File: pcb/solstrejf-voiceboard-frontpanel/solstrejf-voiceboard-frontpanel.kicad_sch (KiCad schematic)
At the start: 13 parts, among them J1 Conn_02x08_Odd_Even, SW1 TRIG

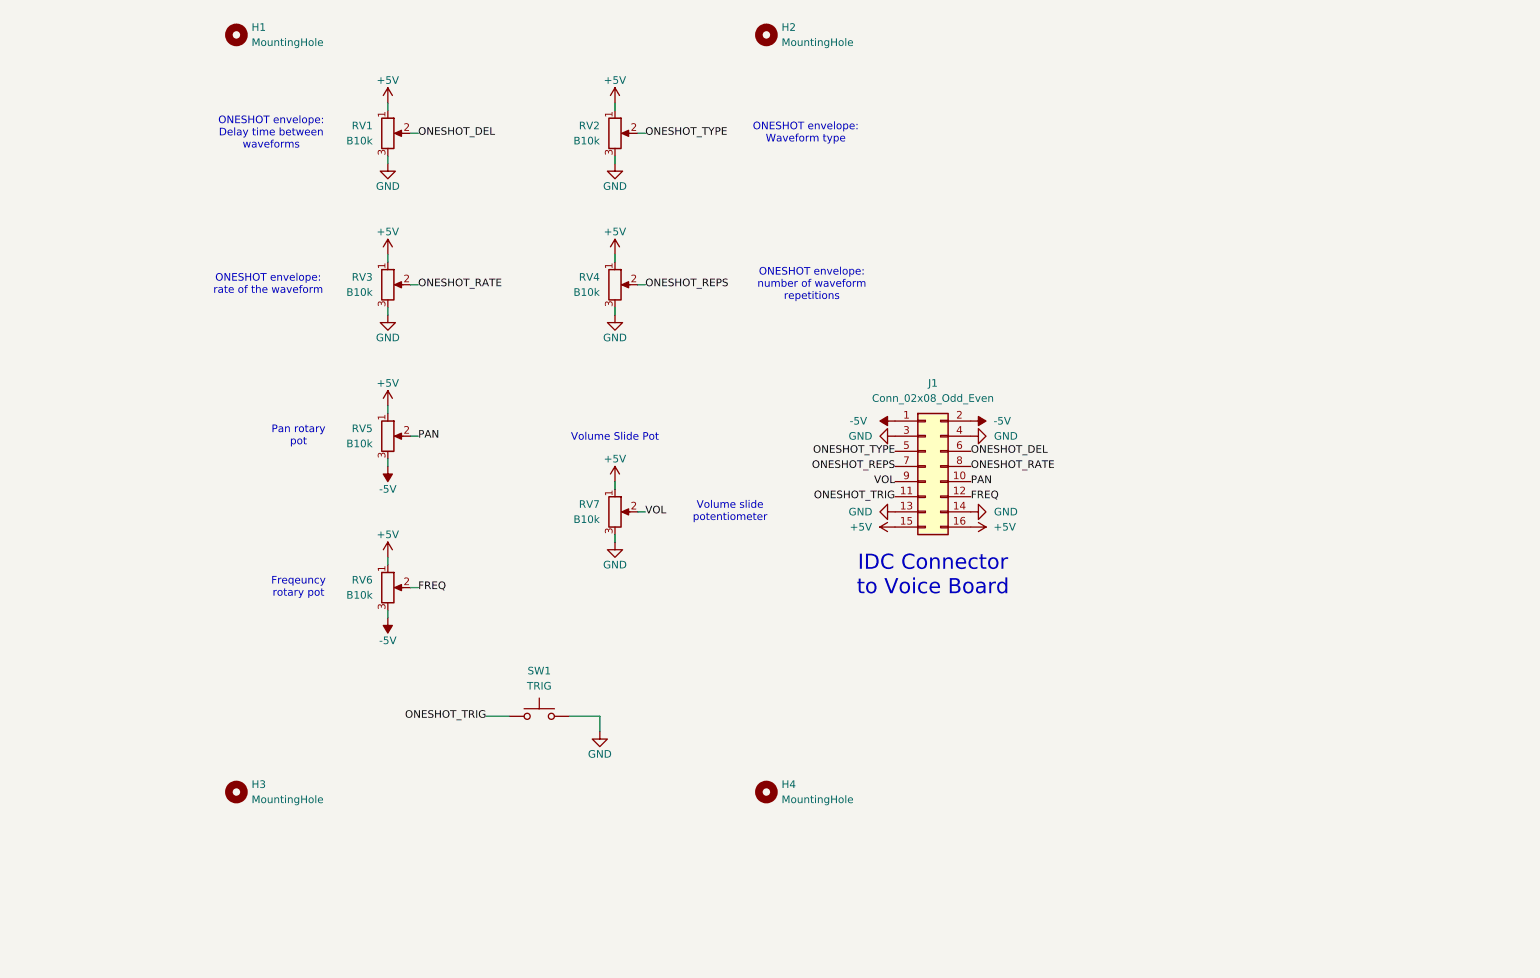
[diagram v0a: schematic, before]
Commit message: updated Kromftronics submodule name and edited path in all PCB projects. Added work-in-progress for the front-panel PCB and the small updates in the voice-board schematic
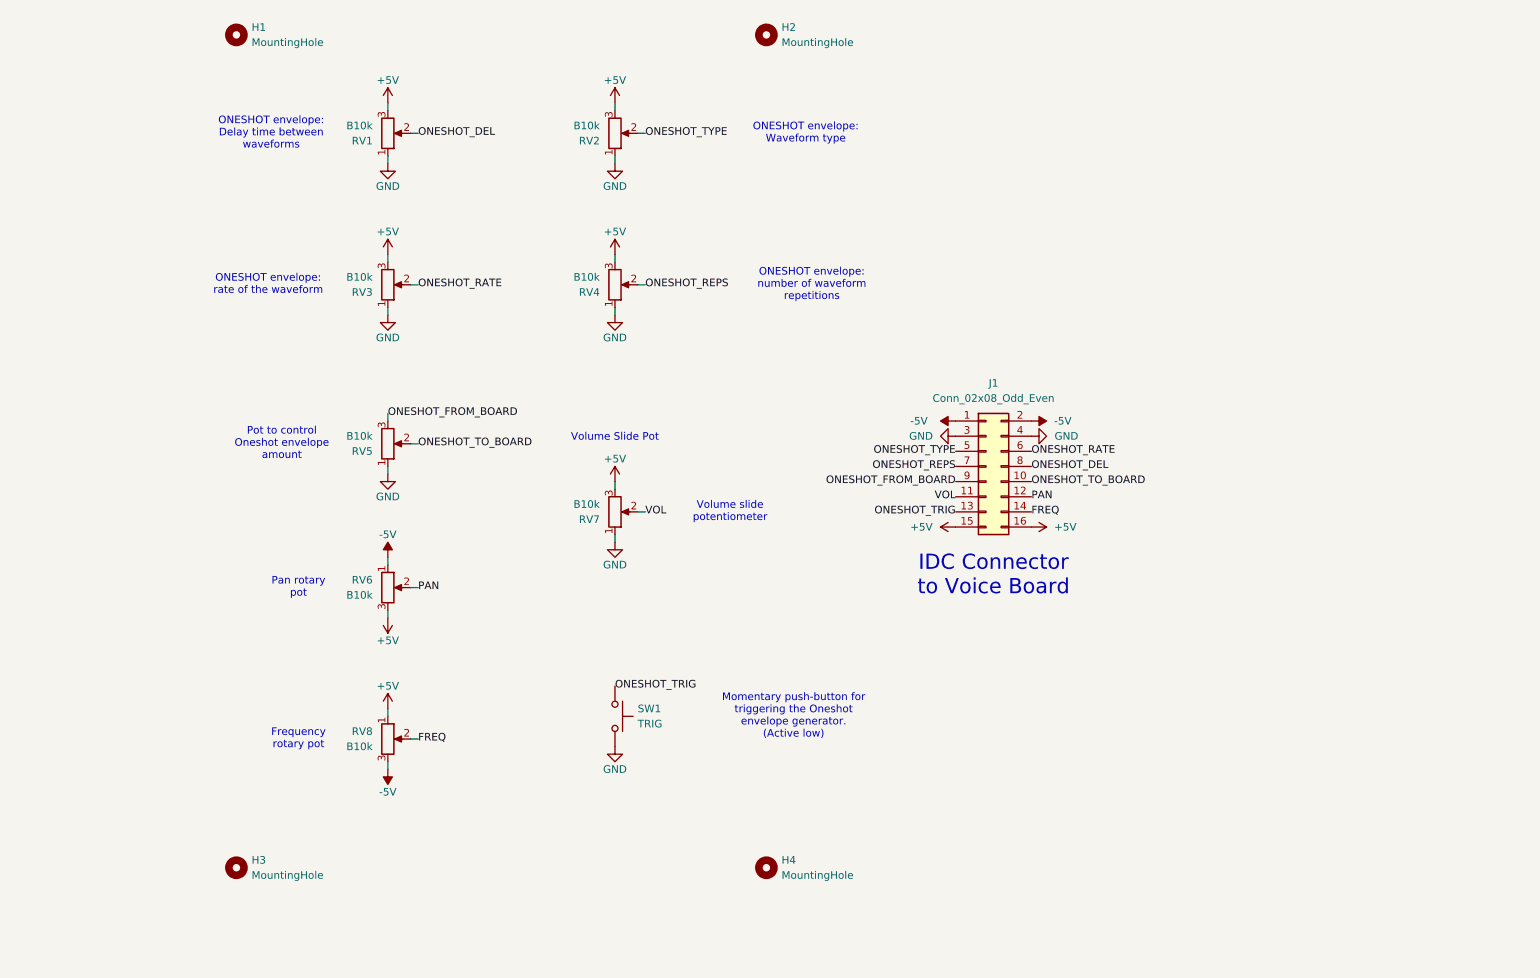
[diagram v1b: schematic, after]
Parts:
- added RV5: B10k, Potentiometer_THT:Potentiometer_Alpha_RD901F-40-00D_Single_Vertical, symbol Device:R_Potentiometer
- renumbered RV5 to RV6, RV6 to RV8
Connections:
- net +5V: now also RV1.3, RV2.3, RV3.3, RV4.3, RV6.3, RV7.3; no longer RV1.1, RV2.1, RV3.1, RV4.1, RV6.1, RV7.1
- net -5V: now also RV6.1; no longer RV6.3
- net FREQ: now also J1.14 (Pin_14); no longer J1.12 (Pin_12)
- net GND: now also RV1.1, RV2.1, RV3.1, RV4.1, RV7.1, RV5.1; no longer J1.13 (Pin_13), J1.14 (Pin_14), RV1.3, RV2.3, RV3.3, RV4.3, RV7.3
- net ONESHOT_DEL: now also J1.8 (Pin_8); no longer J1.6 (Pin_6)
- net ONESHOT_RATE: now also J1.6 (Pin_6); no longer J1.8 (Pin_8)
- net ONESHOT_TRIG: now also J1.13 (Pin_13); no longer J1.11 (Pin_11)
- net PAN: now also J1.12 (Pin_12); no longer J1.10 (Pin_10)
- net VOL: now also J1.11 (Pin_11); no longer J1.9 (Pin_9)
- new net ONESHOT_FROM_BOARD: J1.9 (Pin_9), RV5.3
- new net ONESHOT_TO_BOARD: J1.10 (Pin_10), RV5.2
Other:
- note added: "Frequency rotary pot"
- note added: "Momentary push-button for triggering the Oneshot envelope generator. (Active low)"
- note added: "Pot to control Oneshot envelope amount"
- note removed: "Freqeuncy rotary pot"
- moved on the sheet: H3, H4, J1, RV6, RV8, SW1

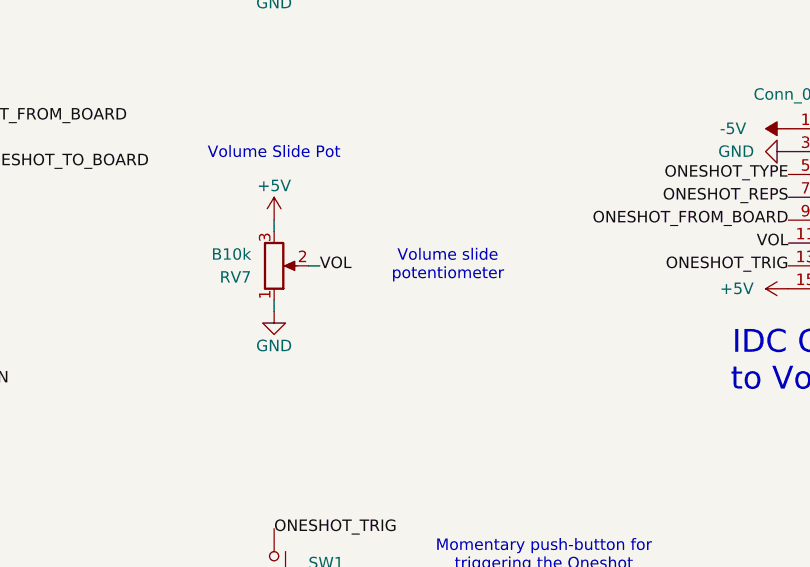
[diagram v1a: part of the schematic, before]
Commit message: Found an error in the front panel where the volume pot was inverted. Updated the schematics of the voice board core and front panel.
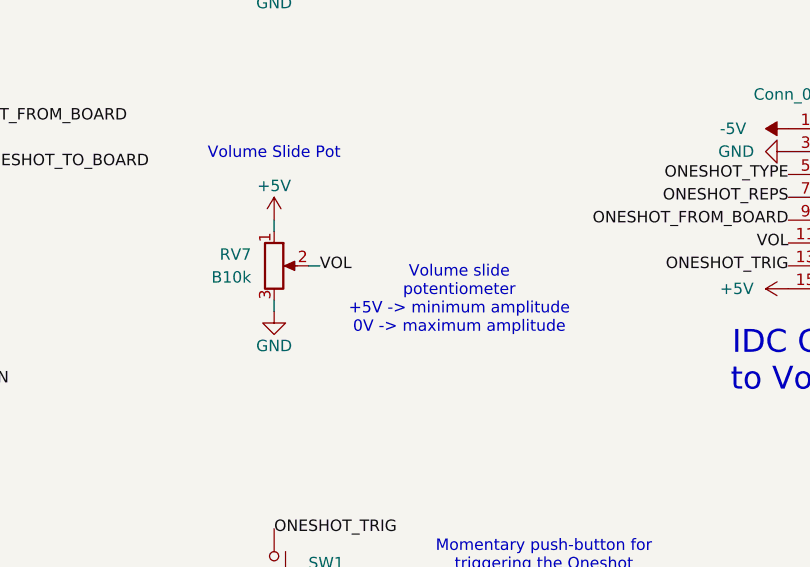
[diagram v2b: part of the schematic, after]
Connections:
- net +5V: now also RV7.1; no longer RV7.3
- net GND: now also RV7.3; no longer RV7.1
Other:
- note added: "Volume slide potentiometer +5V -> minimum amplitude 0V -> maximum amplitude"
- note removed: "Volume slide potentiometer"
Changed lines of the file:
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@@
 	(title_block
 		(title "Solstrejf Voice Board Front Panel")
-		(date "2024-08-31")
+		(date "2024-10-28")
 		(rev "REV 1.0")
 	)
@@
 		)
 	)
-	(text "Volume slide\npotentiometer"
-		(exclude_from_sim no)
-		(at 146.304 118.11 0)
+	(text "Volume slide\npotentiometer\n+5V -> minimum amplitude\n0V -> maximum amplitude"
+		(exclude_from_sim no)
+		(at 147.574 121.92 0)
 		(effects
 			(font
@@
 		(lib_id "Device:R_Potentiometer")
 		(at 127 118.11 0)
-		(mirror x)
-		(unit 1)
-		(exclude_from_sim no)
-		(in_bom yes)
-		(on_board yes)
-		(dnp no)
-		(fields_autoplaced yes)
+		(unit 1)
+		(exclude_from_sim no)
+		(in_bom yes)
+		(on_board yes)
+		(dnp no)
 		(property "Reference" "RV7"
-			(at 124.46 119.3801 0)
+			(at 124.46 116.8399 0)
 			(effects
 				(font
@@
 		)
 		(property "Value" "B10k"
-			(at 124.46 116.8401 0)
-			(effects
-				(font
+			(at 124.46 119.3799 0)
+			(effects
+				(font

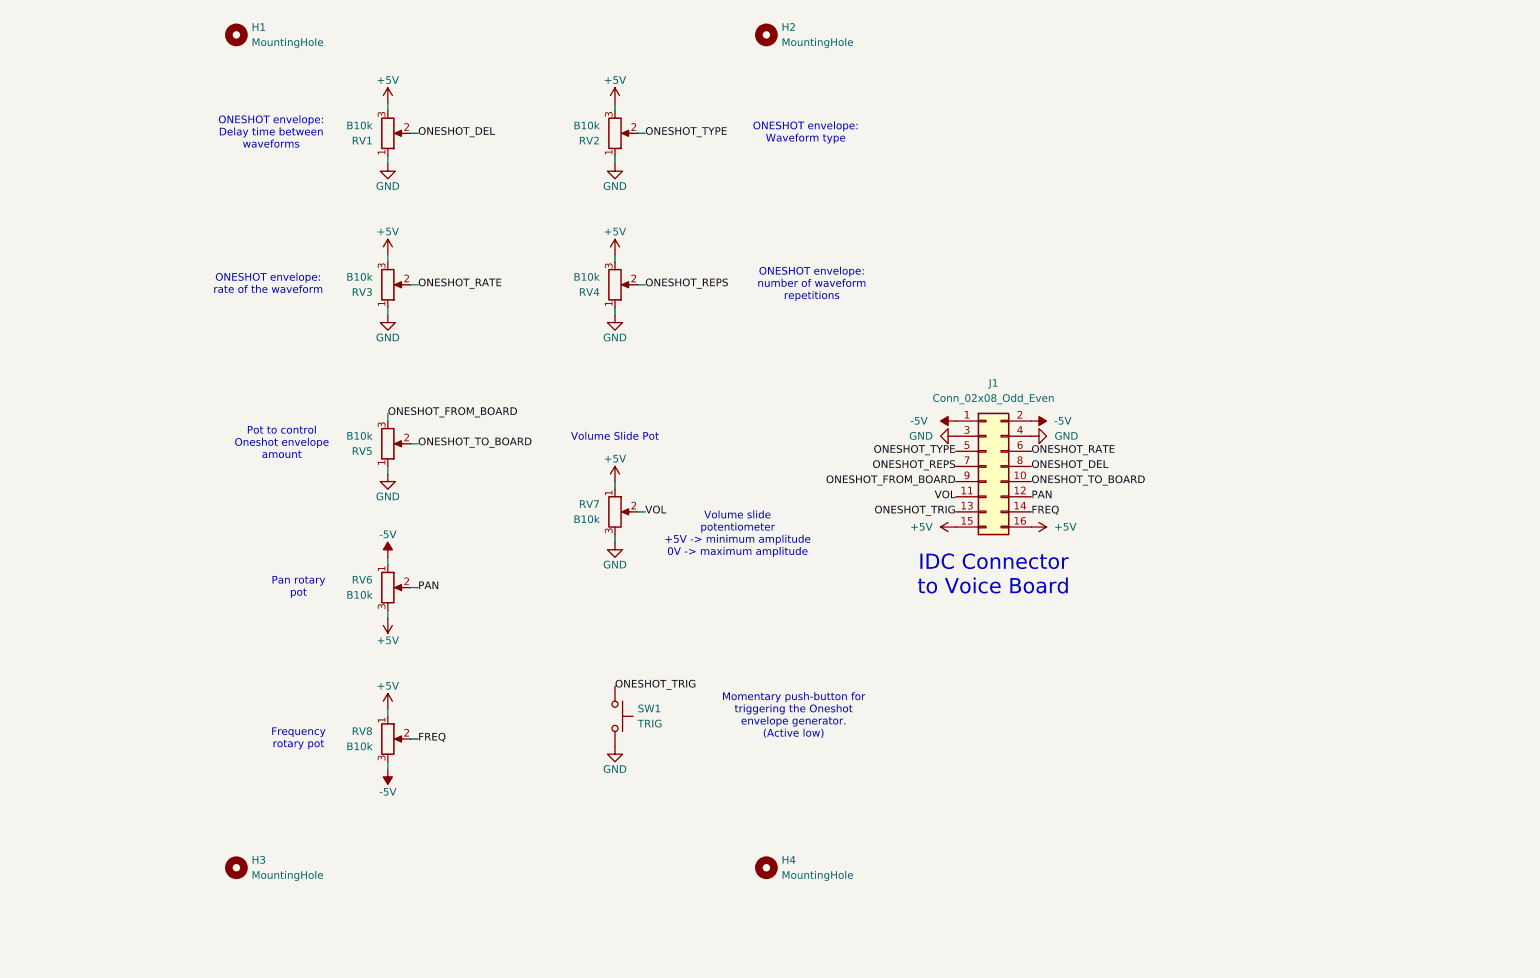
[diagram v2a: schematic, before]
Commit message: updated frontpanel to rev2
- added a external trigger input for PIR motion sensor
- added a 0-5V 1V/oct cv input to the frequency cv
- PCB DRC clean
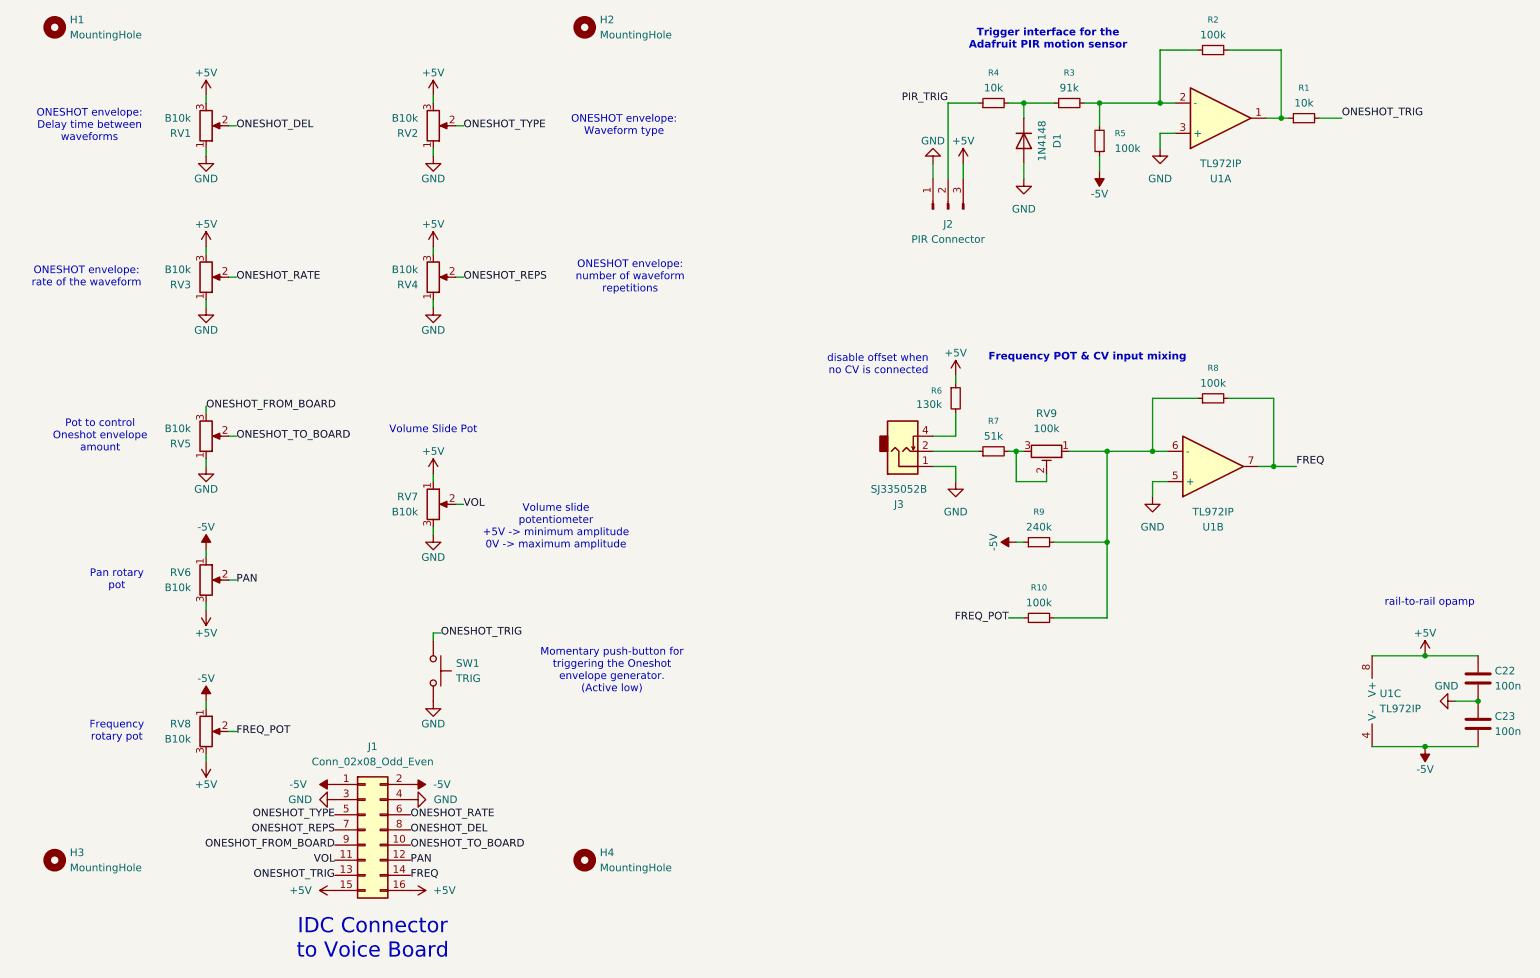
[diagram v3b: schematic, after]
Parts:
- added C22, C23: 100n, Capacitor_THT:C_Disc_D5.0mm_W2.5mm_P5.00mm, symbol Device:C
- added D1: 1N4148, Diode_THT:D_DO-35_SOD27_P7.62mm_Horizontal, symbol Diode:1N4148
- added J2: PIR Connector, Connector_PinHeader_2.54mm:PinHeader_1x03_P2.54mm_Vertical, symbol Connector:Conn_01x03_Pin
- added J3: SJ335052B, Kromftronics_Custom:SJ335052B, symbol Connector_Audio:AudioJack2_SwitchT
- added R1, R4: 10k, Resistor_THT:R_Axial_DIN0207_L6.3mm_D2.5mm_P10.16mm_Horizontal, symbol Device:R_Small
- added R10, R2, R5, R8: 100k, Resistor_THT:R_Axial_DIN0207_L6.3mm_D2.5mm_P10.16mm_Horizontal, symbol Device:R_Small
- added R3: 91k, Resistor_THT:R_Axial_DIN0207_L6.3mm_D2.5mm_P10.16mm_Horizontal, symbol Device:R_Small
- added R6: 130k, Resistor_THT:R_Axial_DIN0207_L6.3mm_D2.5mm_P10.16mm_Horizontal, symbol Device:R_Small
- added R7: 51k, Resistor_THT:R_Axial_DIN0207_L6.3mm_D2.5mm_P10.16mm_Horizontal, symbol Device:R_Small
- added R9: 240k, Resistor_THT:R_Axial_DIN0207_L6.3mm_D2.5mm_P10.16mm_Horizontal, symbol Device:R_Small
- added RV9: 100k, Potentiometer_THT:Potentiometer_Bourns_3296Y_Vertical, symbol Device:R_Potentiometer_Trim
- added U1: TL972IP, Package_DIP:DIP-8_W7.62mm_Socket, symbol Device:Opamp_Dual
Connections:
- net +5V: now also RV8.3, C22.1, J2.3 (Pin_3), R6.1, U1.8 (V+); no longer RV8.1
- net -5V: now also RV8.1, C23.2, R5.1, R9.1, U1.4 (V-); no longer RV8.3
- net FREQ: now also R8.2, U1.7; no longer RV8.2
- net GND: now also C22.2, C23.1, D1.2 (A), J2.1 (Pin_1), J3.1, U1.3 (+), U1.5 (+)
- net ONESHOT_TRIG: now also R1.2
- new net: R10.2, R8.1, R9.2, RV9.1, U1.6 (-)
- new net: D1.1 (K), R3.1, R4.2
- new net: R2.1, R3.2, R5.2, U1.2 (-)
- new net: J3.4, R6.2
- new net: J3.2, R7.1
- new net: R7.2, RV9.2, RV9.3
- new net: R1.1, R2.2, U1.1
- new net FREQ_POT: R10.1, RV8.2
- new net PIR_TRIG: J2.2 (Pin_2), R4.1
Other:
- note added: "Frequency POT & CV input mixing"
- note added: "Trigger interface for the Adafruit PIR motion sensor"
- note added: "disable offset when no CV is connected"
- note added: "rail-to-rail opamp"
- moved on the sheet: H1, H2, H3, H4, J1, RV1, RV2, RV3, RV4, RV5, RV6, RV7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

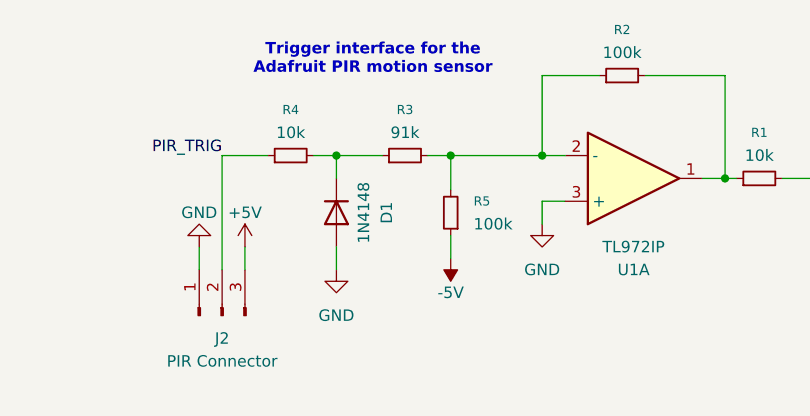
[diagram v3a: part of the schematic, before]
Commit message: updated frontpanel resistor value and added 3D renders
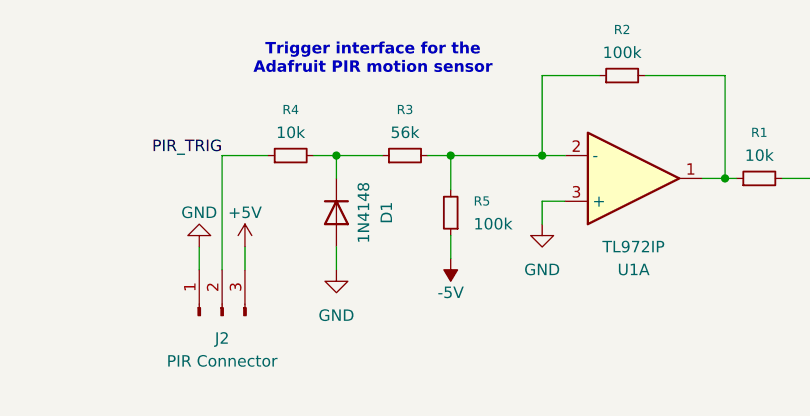
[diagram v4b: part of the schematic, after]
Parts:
- R3: value 91k -> 56k
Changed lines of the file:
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@@
 	(title_block
 		(title "Solstrejf Voice Board Front Panel")
-		(date "2025-11-15")
-		(rev "2.0")
+		(date "2025-12-12")
+		(rev "2.1")
 	)
 	(text "Pan rotary\npot"
@@
 			)
 		)
-		(property "Value" "91k"
+		(property "Value" "56k"
 			(at 203.2 46.99 90)
 			(effects

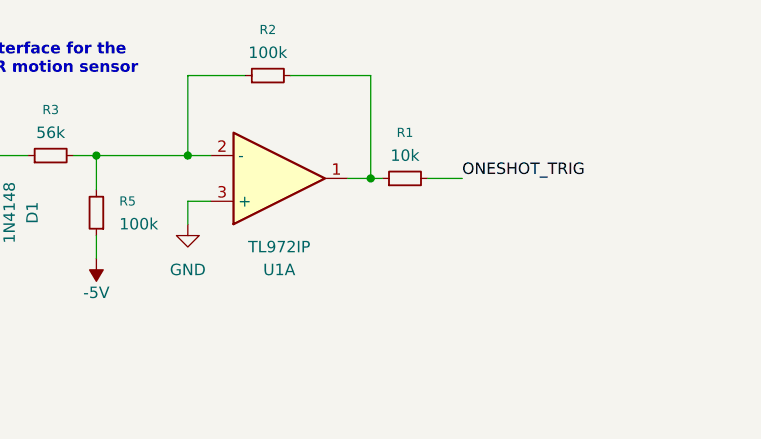
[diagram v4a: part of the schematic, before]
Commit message: updated frontpanel trig opamp output resistor due
- the weak pull-up on the ONESHOT env cause errors with creating zeros
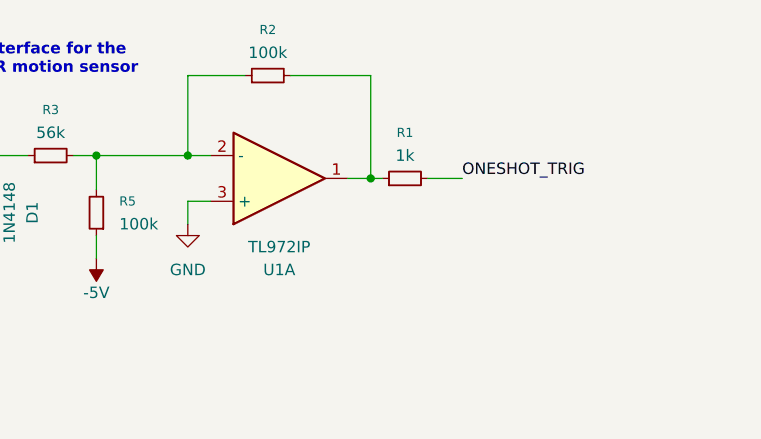
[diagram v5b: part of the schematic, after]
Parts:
- R1: value 10k -> 1k
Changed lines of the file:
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@@
 	(title_block
 		(title "Solstrejf Voice Board Front Panel")
-		(date "2025-12-12")
-		(rev "2.1")
+		(date "2026-01-29")
+		(rev "2.2")
 	)
 	(text "Pan rotary\npot"
@@
 			)
 		)
-		(property "Value" "10k"
+		(property "Value" "1k"
 			(at 242.57 49.53 90)
 			(effects
